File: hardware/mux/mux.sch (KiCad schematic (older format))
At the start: 7 parts, among them J1 Left, J2 Right, U1 TMUX6209

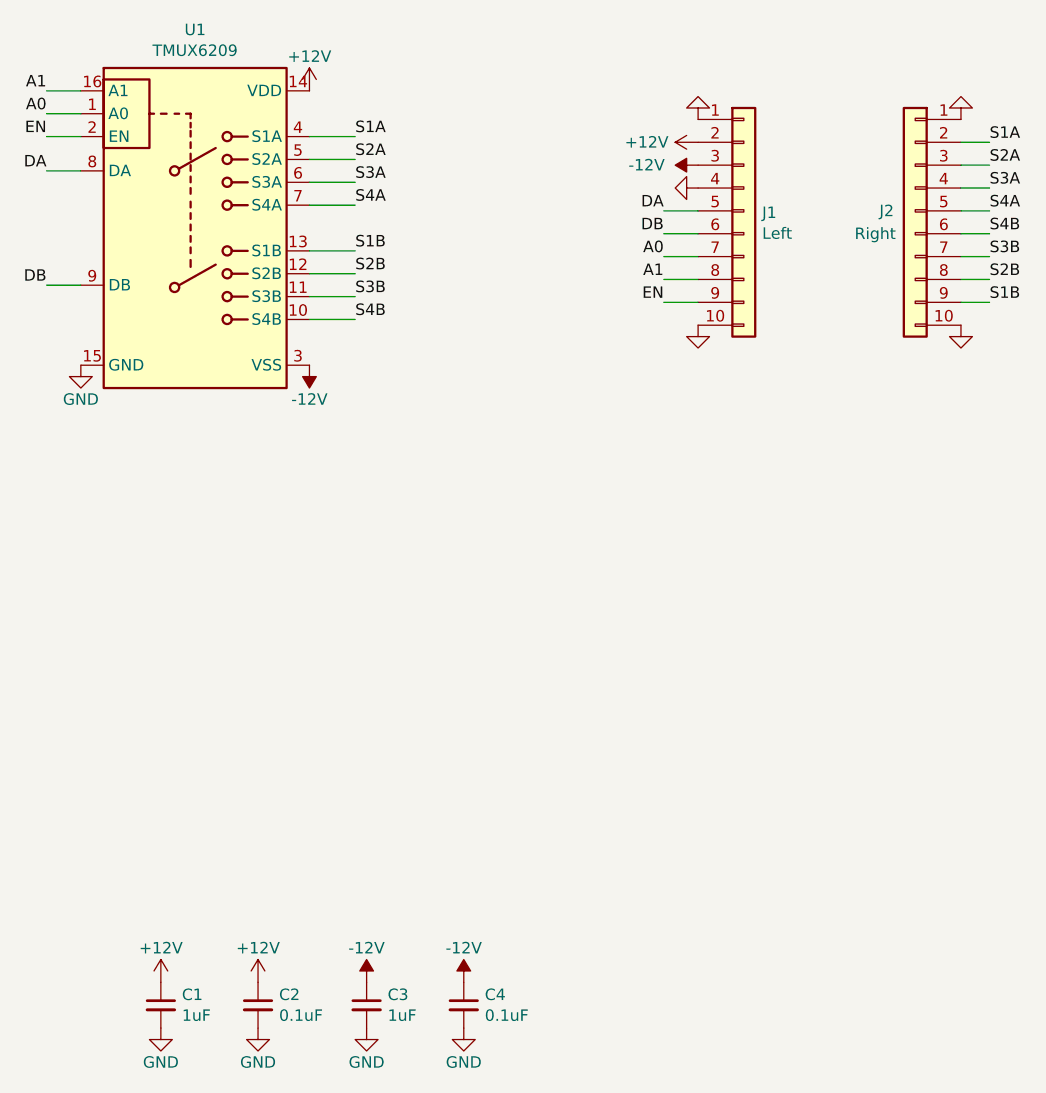
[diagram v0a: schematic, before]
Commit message: Add pull-ups
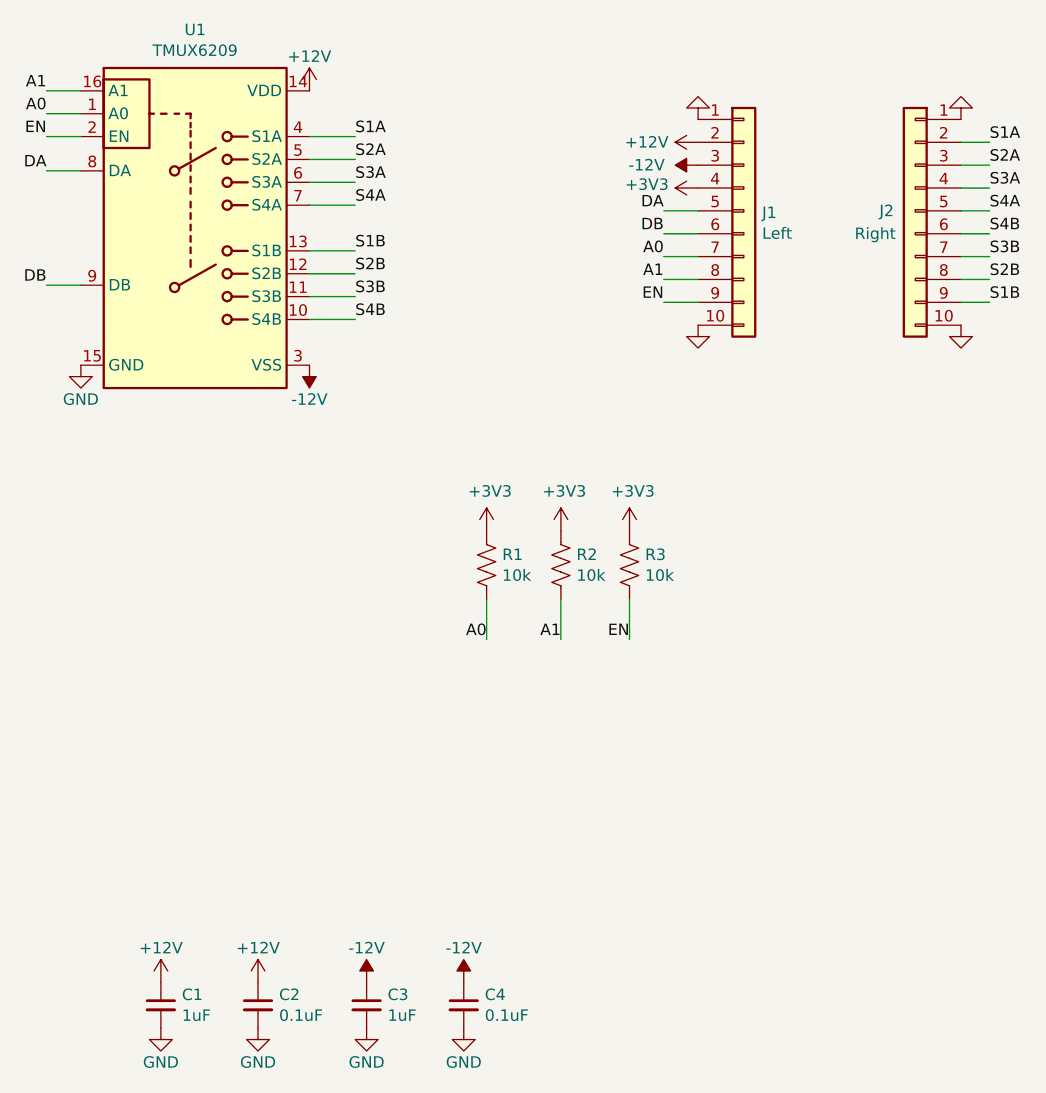
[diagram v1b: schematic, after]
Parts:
- added R1, R2, R3: 10k, Resistor_SMD:R_0603_1608Metric_Pad0.98x0.95mm_HandSolder, symbol Device:R_US
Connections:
- net A0: now also R1.2
- net A1: now also R2.2
- net EN: now also R3.2
- net GND: no longer J1.4 (Pin_4)
- new net +3V3: J1.4 (Pin_4), R1.1, R2.1, R3.1
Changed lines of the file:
@@
-$EndComp
-$Comp
-L power:GND #PWR0118
-U 1 1 615F8F9D
-P 6900 3825
-F 0 "#PWR0118" H 6900 3575 50  0001 C CNN
-F 1 "GND" V 6900 3625 50  0001 C CNN
-F 2 "" H 6900 3825 50  0001 C CNN
-F 3 "" H 6900 3825 50  0001 C CNN
-	1    6900 3825
-	0    1    1    0
 $EndComp
 $Comp
@@
 	1    0    0    -1
 $EndComp
+$Comp
+L Device:R_US R1
+U 1 1 6171C38A
+P 5975 5475
+F 0 "R1" H 6043 5521 50  0000 L CNN
+F 1 "10k" H 6043 5430 50  0000 L CNN
+F 2 "Resistor_SMD:R_0603_1608Metric_Pad0.98x0.95mm_HandSolder" V 6015 5465 50  0001 C CNN
+F 3 "~" H 5975 5475 50  0001 C CNN
+	1    5975 5475
+	1    0    0    -1
+$EndComp
+Text Label 6300 5800 2    50   ~ 0
+A1
+$Comp
+L Device:R_US R2
+U 1 1 6171C7A2
+P 6300 5475
+F 0 "R2" H 6368 5521 50  0000 L CNN
+F 1 "10k" H 6368 5430 50  0000 L CNN
+F 2 "Resistor_SMD:R_0603_1608Metric_Pad0.98x0.95mm_HandSolder" V 6340 5465 50  0001 C CNN
+F 3 "~" H 6300 5475 50  0001 C CNN
+	1    6300 5475
+	1    0    0    -1
+$EndComp
+$Comp
+L Device:R_US R3
+U 1 1 6171D2A1
+P 6600 5475
+F 0 "R3" H 6668 5521 50  0000 L CNN
+F 1 "10k" H 6668 5430 50  0000 L CNN
+F 2 "Resistor_SMD:R_0603_1608Metric_Pad0.98x0.95mm_HandSolder" V 6640 5465 50  0001 C CNN
+F 3 "~" H 6600 5475 50  0001 C CNN
+	1    6600 5475
+	1    0    0    -1
+$EndComp
+$Comp
+L power:+3V3 #PWR0118
+U 1 1 6171DC6B
+P 6300 5325
+F 0 "#PWR0118" H 6300 5175 50  0001 C CNN
+F 1 "+3V3" H 6315 5498 50  0000 C CNN
+F 2 "" H 6300 5325 50  0001 C CNN
+F 3 "" H 6300 5325 50  0001 C CNN
+	1    6300 5325
+	1    0    0    -1
+$EndComp
+$Comp
+L power:+3V3 #PWR0119
+U 1 1 6171E473
+P 6600 5325
+F 0 "#PWR0119" H 6600 5175 50  0001 C CNN
+F 1 "+3V3" H 6615 5498 50  0000 C CNN
+F 2 "" H 6600 5325 50  0001 C CNN
+F 3 "" H 6600 5325 50  0001 C CNN
+	1    6600 5325
+	1    0    0    -1
+$EndComp
+$Comp
+L power:+3V3 #PWR0120
+U 1 1 6171E8E5
+P 5975 5325
+F 0 "#PWR0120" H 5975 5175 50  0001 C CNN
+F 1 "+3V3" H 5990 5498 50  0000 C CNN
+F 2 "" H 5975 5325 50  0001 C CNN
+F 3 "" H 5975 5325 50  0001 C CNN
+	1    5975 5325
+	1    0    0    -1
+$EndComp
+Text Label 5975 5800 2    50   ~ 0
+A0
+Text Label 6600 5800 2    50   ~ 0
+EN
+Wire Wire Line
+	6600 5800 6600 5625
+Wire Wire Line
+	6300 5625 6300 5800
+Wire Wire Line
+	5975 5800 5975 5625
+$Comp
+L power:+3V3 #PWR0121
+U 1 1 61722E69
+P 6900 3825
+F 0 "#PWR0121" H 6900 3675 50  0001 C CNN
+F 1 "+3V3" V 6915 3953 50  0000 L CNN
+F 2 "" H 6900 3825 50  0001 C CNN
+F 3 "" H 6900 3825 50  0001 C CNN
+	1    6900 3825
+	0    -1   -1   0
+$EndComp
 $EndSCHEMATC
